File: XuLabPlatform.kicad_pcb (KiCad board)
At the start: 4 copper layers, 115 x 123 mm, 73 parts, among them J1 SWD Connector, J10 Servo7, J11 Servo8, J12 Thruster SGN, J13 USB_B_Micro, J14 CAN, J15 I2C, J16 UART, J2 Conn_01x04, J3 1986660-2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

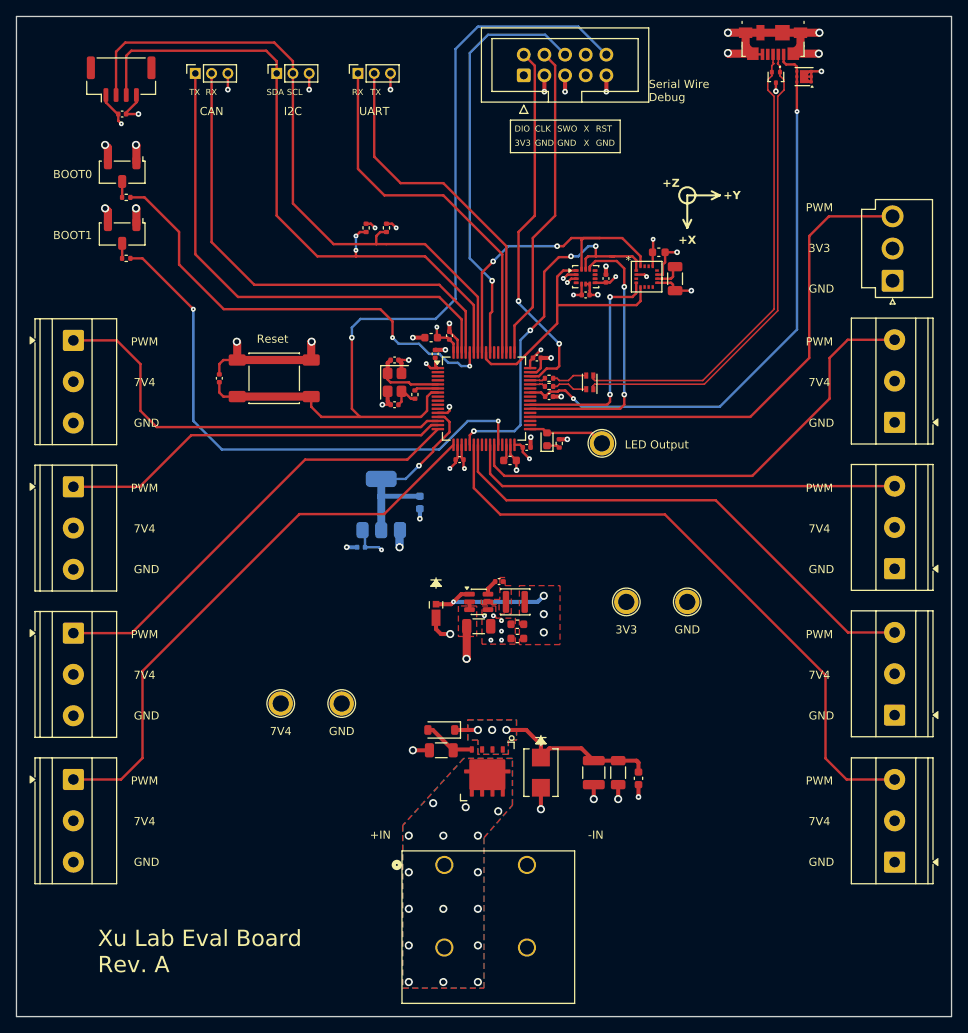
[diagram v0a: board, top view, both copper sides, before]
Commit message: Add return vias and modify silkscreen
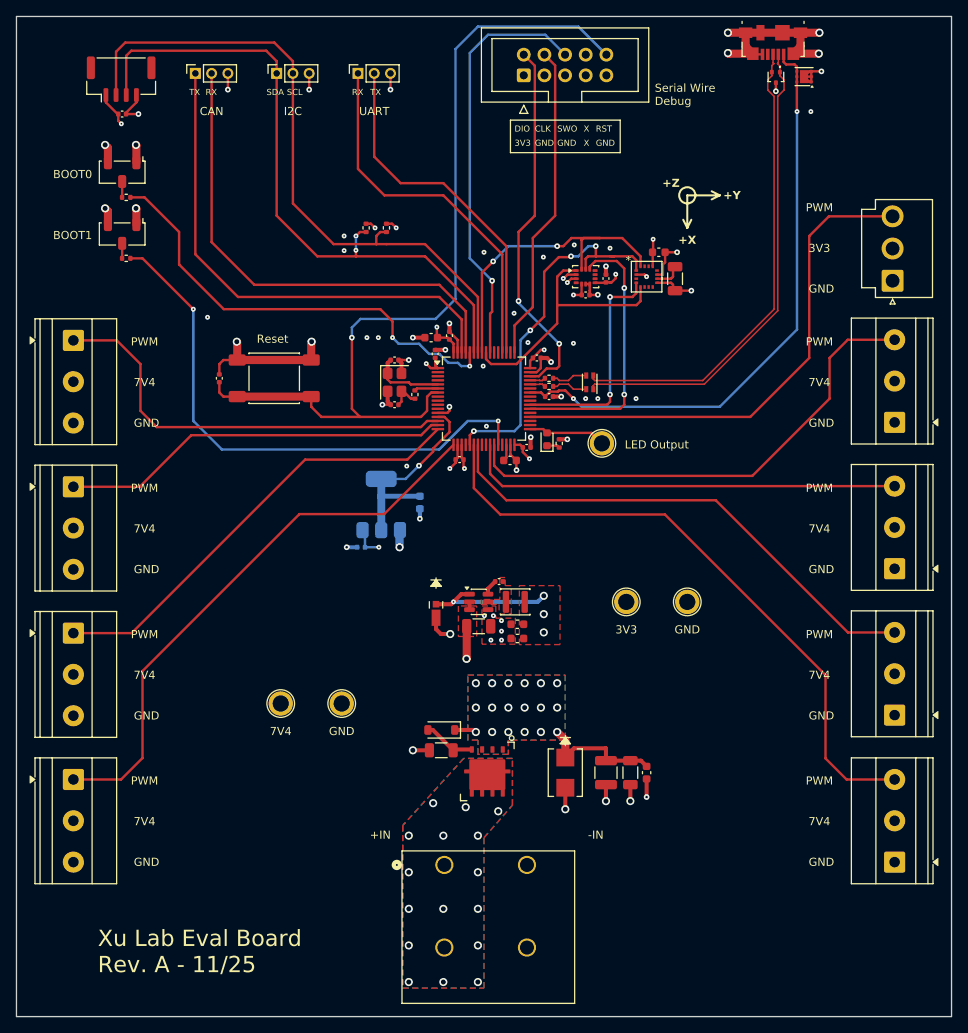
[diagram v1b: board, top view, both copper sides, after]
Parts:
- moved CR1 3.00 mm to (160.0, 126.0)
- moved C18 1.50 mm to (165.0, 126.0)
- moved C19 1.50 mm to (168.0, 126.0)
- moved C20 1.22 mm to (170.0, 126.0)
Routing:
- net +7.4V: track 28.8 -> 23.5 mm, vias 4 -> 19
- net GND: track 135.3 -> 130.7 mm, vias 50 -> 66
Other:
- board text added: "Xu Lab Eval Board Rev. A - 11/25"
- board text removed: "Xu Lab Eval Board Rev. A"

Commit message: Replace zener diode footprints with generics
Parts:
- removed CR1: 7.5V, XuLab:SMB_DIO
- removed CR2: 3.3V, XuLab:DO-219AD_VIS
- added D4: 7.5V, Diode_SMD:D_SMB, F.Cu at (160.0, 126.0)
- added D5: 3.3V, Diode_SMD:D_MicroSMP_KA, F.Cu at (161.0, 107.0)
- renumbered D3 to D2, D2 to D3
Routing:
- net +7.4V: track 23.5 -> 21.5 mm
- net +3.3V: track 58.7 -> 60.3 mm
- net GND: track 130.7 -> 129.1 mm
- added copper zone on B.Cu, net +3.3V

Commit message: Add ferrite bead and decoupling capacitors to analog power input
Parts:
- added C26: 1uF, Capacitor_SMD:C_0603_1608Metric, B.Cu at (147.6, 82.8)
- added C27: 100nF, Capacitor_SMD:C_0402_1005Metric, B.Cu at (147.1, 84.1)
- added FB1: 120 Ohms @ 100 MHz, Inductor_SMD:L_0805_2012Metric, B.Cu at (143.0, 86.0)
- C7: value 100nF -> 10uF; footprint Capacitor_SMD:C_0402_1005Metric -> Capacitor_SMD:C_1206_3216Metric
- C8: value 1uF -> 10uF; footprint Capacitor_SMD:C_0603_1608Metric -> Capacitor_SMD:C_1206_3216Metric
- U6: value TLV1117LV33 -> TLV1117-33
- moved C8 15.1 mm to (130.0, 101.8), turned to 180 degrees
- moved U6 12.0 mm to (137.0, 105.0)
- moved C7 10.8 mm to (130.7, 108.2)
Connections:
- C7 pad 1: +3.3V -> +7.4V
- C8 pad 1: +3.3VA -> Net-(U6-VO)
- U6 pad 2: +3.3VA -> Net-(U6-VO)
- U6 pad 3: +3.3V -> +7.4V
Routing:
- net Net-(U6-VO): track 0.00 -> 31.7 mm
- net +3.3VA: track 25.0 -> 8.17 mm
- net +7.4V: track 21.5 -> 28.3 mm, vias 19 -> 20
- net /MCU A/BOOT1: track 67.4 -> 63.2 mm
- net GND: track 129.1 -> 133.3 mm, vias 66 -> 67
- net +3.3V: track 60.3 -> 56.4 mm, vias 19 -> 18

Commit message: Add 3.3 V voltage divider to 5 V VBUS line
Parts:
- added R10: 10k, Resistor_SMD:R_0603_1608Metric, B.Cu at (177.5, 79.5)
- added R11: 20k, Resistor_SMD:R_0603_1608Metric, B.Cu at (177.5, 81.0)
- moved C7 4.05 mm to (130.6, 104.2)
- moved C8 4.05 mm to (129.9, 97.8)
- moved U6 4.05 mm to (136.9, 101.0)
- moved FL1 0.73 mm to (163.2, 77.3)
- moved C25 0.25 mm to (158.0, 80.0)
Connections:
- J13 pad 1: /MCU A/USB_VBUS -> /MCU A/USB_VBUS_I
- U5 pad 4: /MCU A/USB_VBUS -> /MCU A/USB_VBUS_I
- U5 pad 5: /MCU A/USB_VBUS -> /MCU A/USB_VBUS_I
- U5 pad 6: /MCU A/USB_VBUS -> /MCU A/USB_VBUS_I
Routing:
- net /MCU A/USB_VBUS: track 73.2 -> 23.8 mm, vias 2 -> 1
- net /MCU A/USB_VBUS_I: track 0.00 -> 48.6 mm, vias 0 -> 1
- net +7.4V: track 28.3 -> 32.3 mm
- net Net-(U6-VO): track 31.7 -> 27.7 mm
- net GND: track 133.3 -> 135.5 mm, vias 67 -> 68
- net /MCU A/USB_D_I+: track 58.4 -> 57.0 mm
- net /MCU A/USB_D_I-: track 59.2 -> 57.7 mm

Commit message: Remove LDO and connect FB to switching output
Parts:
- removed the C7 at (130.6, 104.2)
- removed the C8 at (129.9, 97.8)
- removed U6: TLV1117-33, Package_TO_SOT_SMD:SOT-223-3_TabPin2
- renumbered C26 to C7, C27 to C8
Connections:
- FB1 pad 2: Net-(U6-VO) -> +3.3V
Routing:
- net Net-(U6-VO): track 27.7 -> 0.00 mm
- net +7.4V: track 32.3 -> 21.5 mm, vias 20 -> 19
- net GND: track 135.5 -> 128.6 mm, vias 68 -> 65
- net +3.3V: track 56.4 -> 58.3 mm, vias 18 -> 19

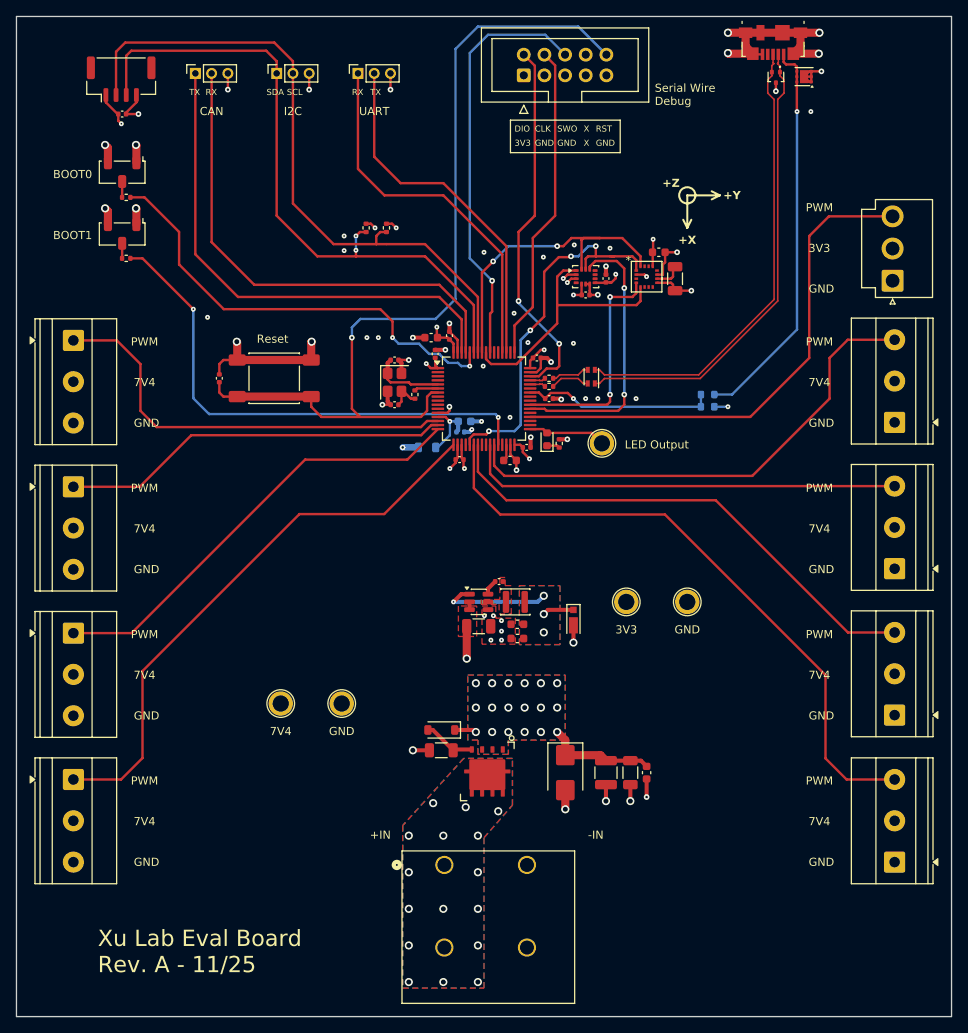
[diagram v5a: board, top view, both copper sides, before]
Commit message: Change IMU to BMI088
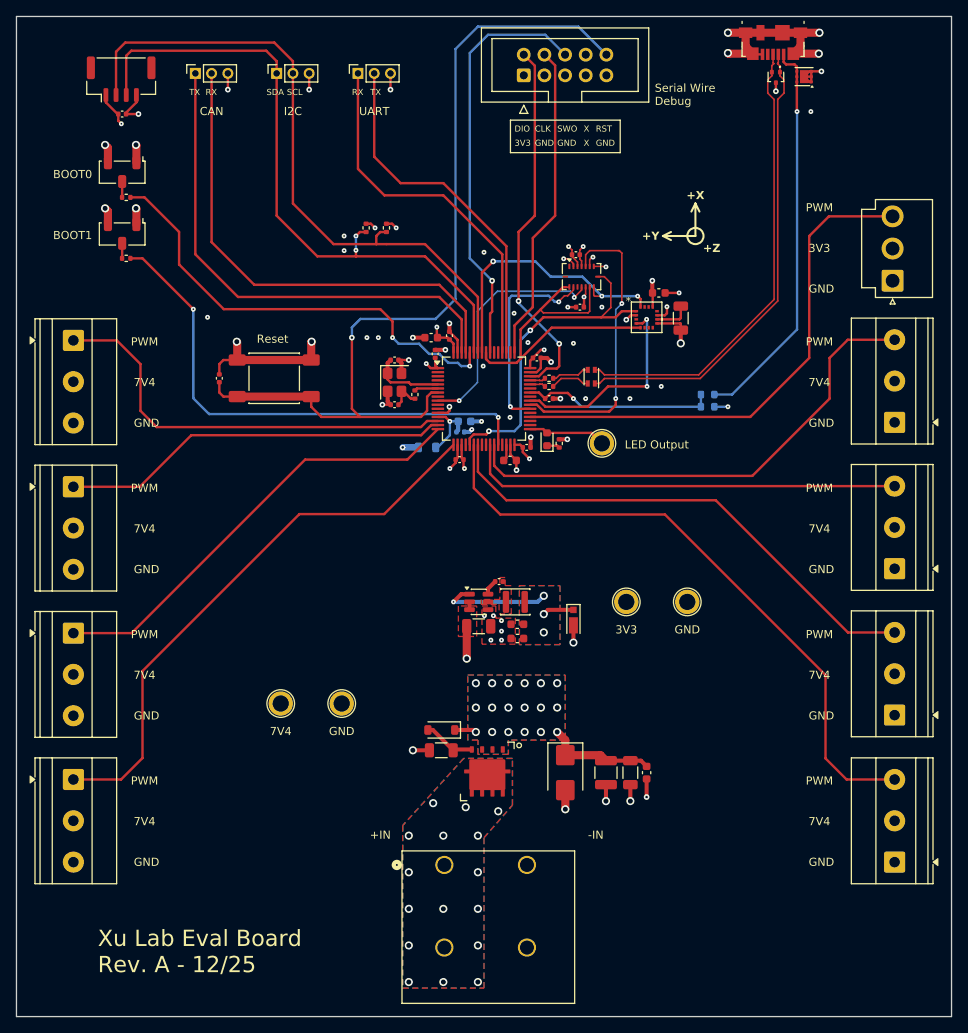
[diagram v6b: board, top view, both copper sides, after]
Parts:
- U2: value ISM330DHCX -> BMI088; footprint Package_LGA:LGA-14_3x2.5mm_P0.5mm_LayoutBorder3x4y -> Package_LGA:Bosch_LGA-16_4.5x3mm_P0.5mm_LayoutBorder7x1y_ClockwisePinNumbering
- moved C14 5.09 mm to (161.3, 62.3)
- moved C15 5.00 mm to (171.5, 67.0)
- moved U3 5.00 mm to (170.0, 70.0)
- moved C16 4.90 mm to (174.2, 70.1)
- moved C13 4.76 mm to (161.8, 68.8), turned to 180 degrees
- moved U2 0.50 mm to (162.0, 65.0)
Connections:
- U1 pad 10: unconnected-(U1-PC2-Pad10) -> /MCU A/GPIO_EXTI2
- U1 pad 11: unconnected-(U1-PC3-Pad11) -> /MCU A/GPIO_EXTI3
- U1 pad 40: unconnected-(U1-PC9-Pad40) -> /SPI1_CS3
- U1 pad 9: /MCU A/GPIO_EXTI1 -> /GPIO_EXTI1
- U2 pad 1: /SPI1_MISO -> /Attitude and Heading Module/ACCL_INT2
- U2 pad 10: unconnected-(U2-OCS_AUX-Pad10) -> /SPI1_MISO
- U2 pad 11: unconnected-(U2-SDO_AUX-Pad11) -> +3.3V
- U2 pad 12: /SPI1_CS1 -> /GPIO_EXTI1
- U2 pad 13: /SPI1_SCK -> /Attitude and Heading Module/GYRO_INT2
- U2 pad 14: /SPI1_MOSI -> /SPI1_CS1
- U2 pad 3: GND -> +3.3V
- U2 pad 4: unconnected-(U2-INT1-Pad4) -> GND
- U2 pad 5: +3.3V -> /SPI1_CS2
- U2 pad 8: +3.3V -> /SPI1_SCK
- U2 pad 9: unconnected-(U2-INT2-Pad9) -> /SPI1_MOSI
- U3 pad 4: /SPI1_CS2 -> /SPI1_CS3
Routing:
- net /GPIO_EXTI1: track 0.00 -> 29.6 mm, vias 0 -> 2
- net /SPI1_CS3: track 0.00 -> 25.5 mm, vias 0 -> 2
- net /SPI1_MISO: track 32.5 -> 42.9 mm
- net /SPI1_CS2: track 27.6 -> 36.4 mm
- net /SPI1_CS1: track 34.0 -> 25.3 mm
- net /SPI1_SCK: track 46.4 -> 40.5 mm, vias 4 -> 2
- net /SPI1_MOSI: track 39.2 -> 34.9 mm, vias 2 -> 3
- net Net-(U3-CAP): track 3.41 -> 4.46 mm
- net GND: track 128.6 -> 129.1 mm
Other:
- board text added: "Xu Lab Eval Board Rev. A - 12/25"
- board text removed: "Xu Lab Eval Board Rev. A - 11/25"
